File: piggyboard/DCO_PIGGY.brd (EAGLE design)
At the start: 100 x 22 mm, 7 parts, among them P1 100KB, P2 100KB, P3 100KB

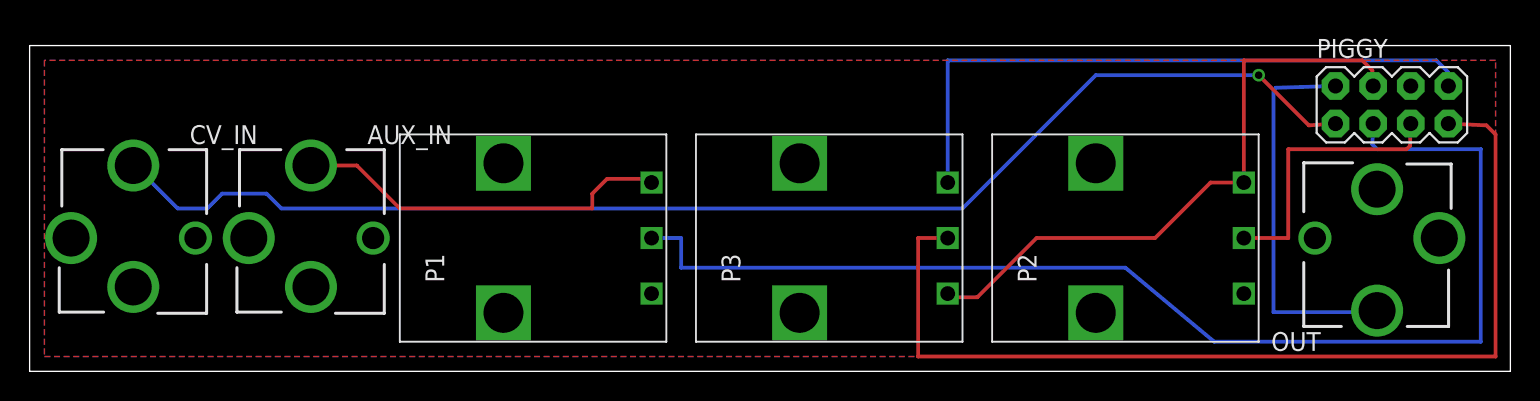
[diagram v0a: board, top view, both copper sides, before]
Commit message: Changed isolation settings on ground planes for piggy back board
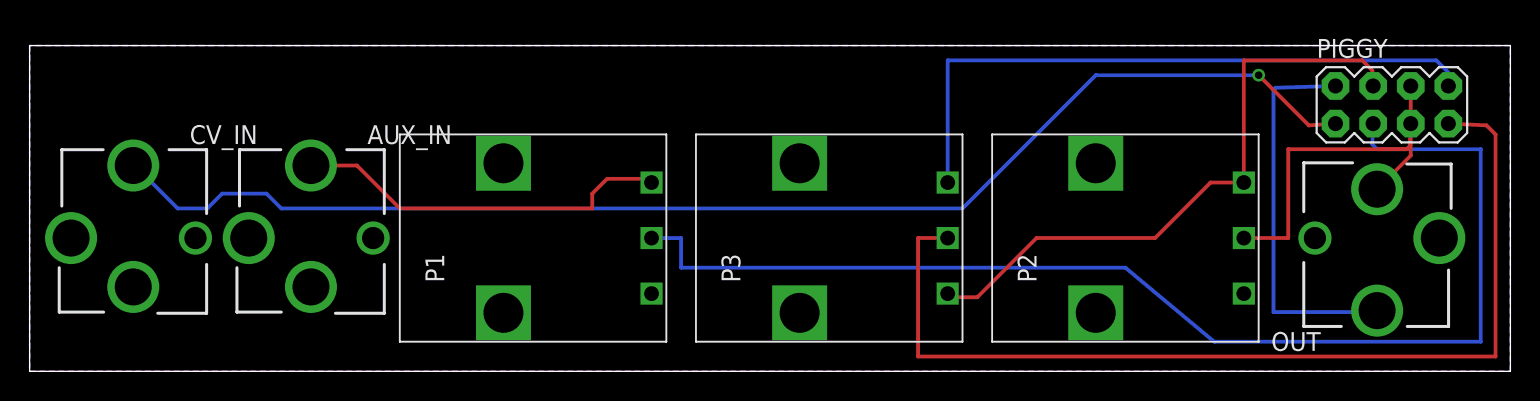
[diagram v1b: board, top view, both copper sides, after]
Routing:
- net GND: track 0.00 -> 7.91 mm
- added copper zone on layer 1, net GND
- added copper zone on layer 16, net N$1
- removed copper zone on layer 1, net N$1
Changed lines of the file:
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@@
 <setting verticaltext="up"/>
 </settings>
-<grid distance="1" unitdist="mm" unit="mm" style="lines" multiple="1" display="yes" altdistance="0.1" altunitdist="mm" altunit="mm"/>
+<grid distance="0.05" unitdist="inch" unit="inch" style="lines" multiple="1" display="yes" altdistance="0.005" altunitdist="inch" altunit="inch"/>
 <layers>
 <layer number="1" name="Top" color="4" fill="1" visible="yes" active="yes"/>
@@
 <contactref element="P1" pad="1"/>
 <contactref element="P2" pad="1"/>
-<polygon width="0.254" layer="16">
-<vertex x="1" y="21"/>
-<vertex x="1" y="1"/>
-<vertex x="99" y="1"/>
-<vertex x="99" y="21"/>
+<polygon width="0.254" layer="16" isolate="0.254">
+<vertex x="0" y="22"/>
+<vertex x="0" y="0"/>
+<vertex x="100" y="0"/>
+<vertex x="100" y="22"/>
 </polygon>
+<polygon width="0.254" layer="1" isolate="0.254">
+<vertex x="0" y="22"/>
+<vertex x="0" y="0"/>
+<vertex x="100" y="0"/>
+<vertex x="100" y="22"/>
+</polygon>
+<wire x1="93.27" y1="19.27" x2="93.27" y2="14.57" width="0.254" layer="1"/>
+<wire x1="93.27" y1="14.57" x2="91" y2="12.3" width="0.254" layer="1"/>
 </signal>
 <signal name="OUT">
@@
 </signal>
 <signal name="N$1">
-<polygon width="0.254" layer="1">
-<vertex x="1" y="21"/>
-<vertex x="1" y="1"/>
-<vertex x="99" y="1"/>
-<vertex x="99" y="21"/>
+<polygon width="0.254" layer="16" isolate="0.254">
+<vertex x="0" y="22"/>
+<vertex x="0" y="0"/>
+<vertex x="100" y="0"/>
+<vertex x="100" y="22"/>
 </polygon>
 </signal>

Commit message: fix for a messed up output jack on the piggy board
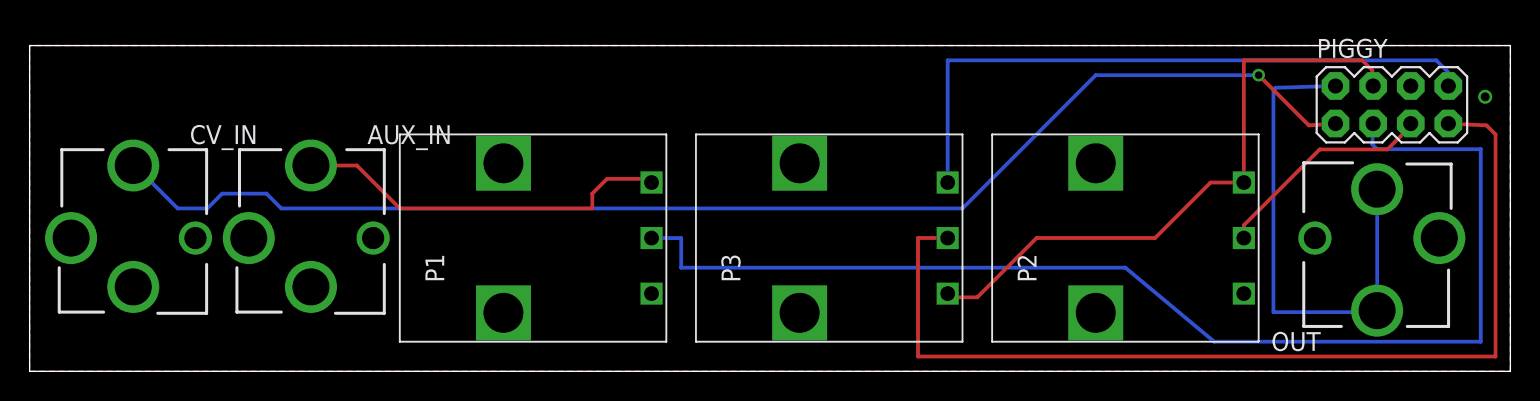
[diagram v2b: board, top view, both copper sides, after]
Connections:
- net GND: no longer OUT.2
- net OUT: now also OUT.2
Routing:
- net OUT: track 26.4 -> 34.6 mm
- net GND: track 7.91 -> 0.00 mm, vias 0 -> 1
- net COARSE: track 18.8 -> 15.1 mm
- removed copper zone on layer 16, net N$1
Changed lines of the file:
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@@
 <?xml version="1.0" encoding="utf-8"?>
 <!DOCTYPE eagle SYSTEM "eagle.dtd">
-<eagle version="6.1">
+<eagle version="6.4">
 <drawing>
 <settings>
@@
 <setting verticaltext="up"/>
 </settings>
-<grid distance="0.05" unitdist="inch" unit="inch" style="lines" multiple="1" display="yes" altdistance="0.005" altunitdist="inch" altunit="inch"/>
+<grid distance="1" unitdist="mm" unit="mm" style="lines" multiple="1" display="yes" altdistance="0.1" altunitdist="mm" altunit="mm"/>
 <layers>
 <layer number="1" name="Top" color="4" fill="1" visible="yes" active="yes"/>
@@
 </class>
 </classes>
-<designrules>
+<designrules name="default">
 <description language="de">&lt;b&gt;EAGLE Design Rules&lt;/b&gt;
 &lt;p&gt;
@@
 <contactref element="OUT" pad="1@1"/>
 <contactref element="OUT" pad="1@2"/>
-<contactref element="OUT" pad="2"/>
 <contactref element="P1" pad="1"/>
 <contactref element="P2" pad="1"/>
-<polygon width="0.254" layer="16" isolate="0.254">
-<vertex x="0" y="22"/>
-<vertex x="0" y="0"/>
-<vertex x="100" y="0"/>
-<vertex x="100" y="22"/>
-</polygon>
 <polygon width="0.254" layer="1" isolate="0.254">
 <vertex x="0" y="22"/>
@@
 <vertex x="100" y="22"/>
 </polygon>
-<wire x1="93.27" y1="19.27" x2="93.27" y2="14.57" width="0.254" layer="1"/>
-<wire x1="93.27" y1="14.57" x2="91" y2="12.3" width="0.254" layer="1"/>
+<via x="98.298" y="18.542" extent="1-16" drill="0.6" shape="square"/>
+<polygon width="0.254" layer="16">
+<vertex x="0" y="22"/>
+<vertex x="0" y="0"/>
+<vertex x="100" y="0"/>
+<vertex x="100" y="22"/>
+</polygon>
 </signal>
 <signal name="OUT">
@@
 <wire x1="84" y1="4" x2="91" y2="4" width="0.254" layer="16"/>
 <wire x1="91" y1="4.1" x2="91" y2="4" width="0.254" layer="16"/>
+<contactref element="OUT" pad="2"/>
+<wire x1="91" y1="12.3" x2="91" y2="4.1" width="0.254" layer="16"/>
 </signal>
 <signal name="CV_IN">
@@
 <contactref element="PIGGY" pad="5"/>
 <contactref element="P2" pad="2"/>
-<wire x1="93.27" y1="16.73" x2="93.22" y2="15.22" width="0.254" layer="1"/>
-<wire x1="93.22" y1="15.22" x2="93" y2="15" width="0.254" layer="1"/>
-<wire x1="93" y1="15" x2="85" y2="15" width="0.254" layer="1"/>
-<wire x1="85" y1="15" x2="85" y2="9" width="0.254" layer="1"/>
-<wire x1="85" y1="9" x2="82" y2="9" width="0.254" layer="1"/>
+<wire x1="82" y1="9" x2="82" y2="9.864" width="0.254" layer="1"/>
+<wire x1="82" y1="9.864" x2="87.122" y2="14.986" width="0.254" layer="1"/>
+<wire x1="87.122" y1="14.986" x2="91.694" y2="14.986" width="0.254" layer="1"/>
+<wire x1="91.694" y1="14.986" x2="92.964" y2="16.256" width="0.254" layer="1"/>
+<wire x1="92.964" y1="16.256" x2="92.964" y2="16.424" width="0.254" layer="1"/>
+<wire x1="92.964" y1="16.424" x2="93.27" y2="16.73" width="0.254" layer="1"/>
 </signal>
 <signal name="FINE">
@@
 <wire x1="42" y1="13" x2="42" y2="12.75" width="0.254" layer="1"/>
 </signal>
-<signal name="N$1">
-<polygon width="0.254" layer="16" isolate="0.254">
-<vertex x="0" y="22"/>
-<vertex x="0" y="0"/>
-<vertex x="100" y="0"/>
-<vertex x="100" y="22"/>
-</polygon>
-</signal>
 </signals>

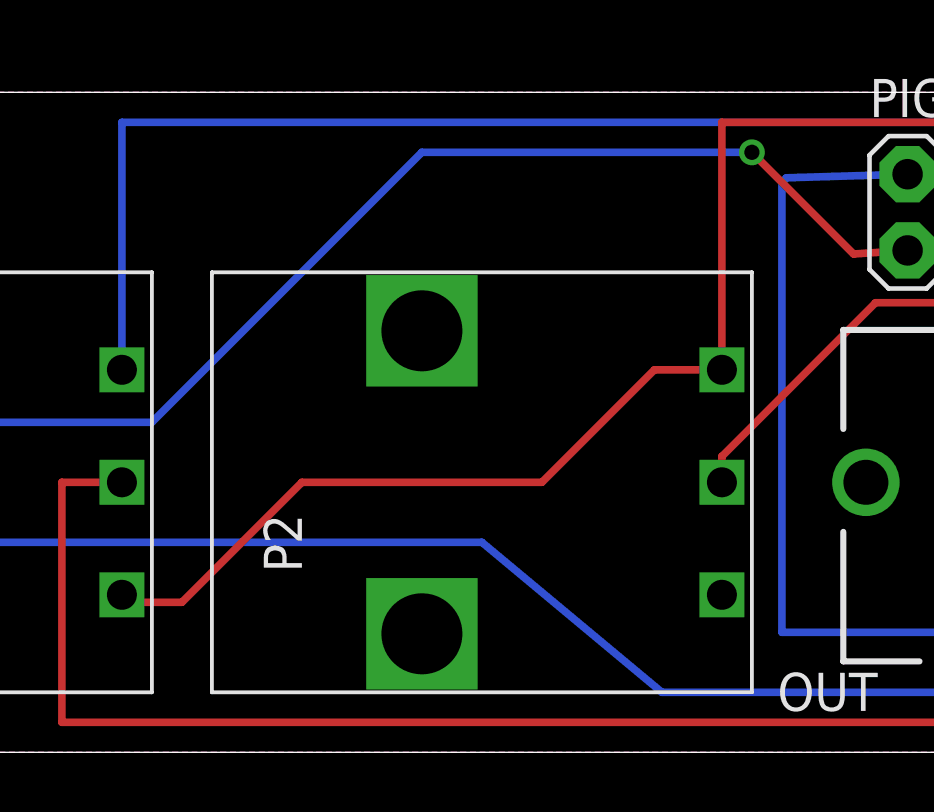
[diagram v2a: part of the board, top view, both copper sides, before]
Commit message: fixed footprint
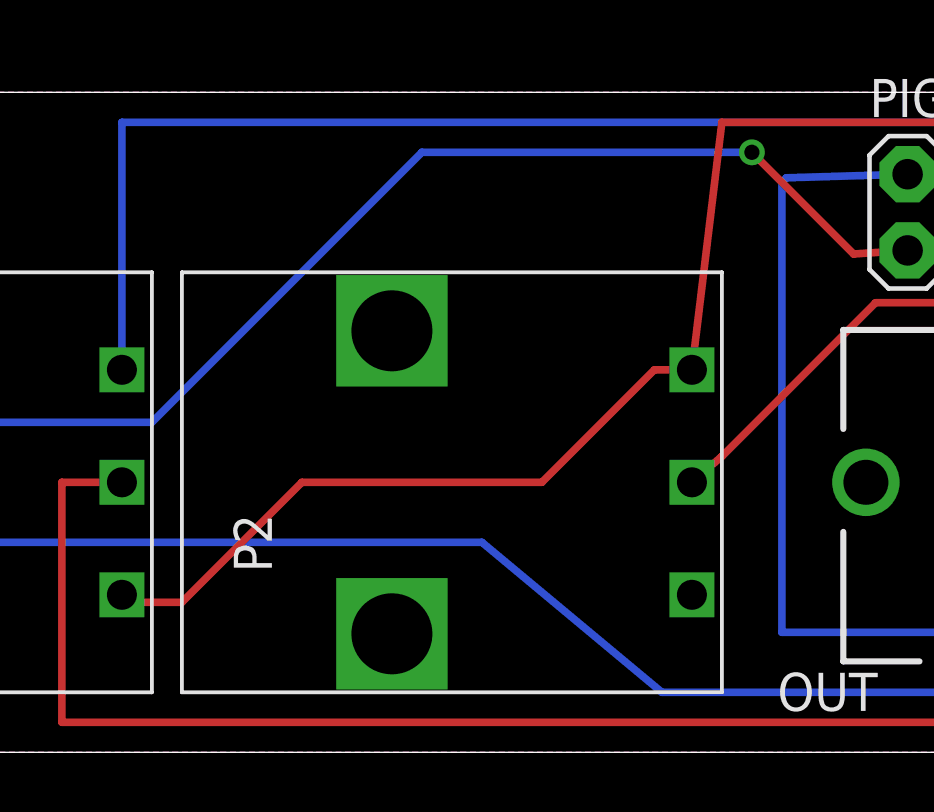
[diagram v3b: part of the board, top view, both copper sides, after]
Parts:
- moved P2 6.00 mm to (71.0, 9.00)
- moved P1 5.00 mm to (32.0, 9.00)
- moved P3 5.00 mm to (52.0, 9.00)
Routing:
- net +5V: track 41.7 -> 40.8 mm
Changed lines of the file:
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@@
 <element name="AUX_IN" library="erthenvar" package="ERTHENVAR-JACK" value="AUDIO-JACKERTHENVAR" x="19" y="9"/>
 <element name="OUT" library="erthenvar" package="ERTHENVAR-JACK" value="AUDIO-JACKERTHENVAR" x="91" y="9" rot="R180"/>
-<element name="P1" library="SparkFun" package="PDB12" value="100KB" x="37" y="9" rot="R90"/>
-<element name="P2" library="SparkFun" package="PDB12" value="100KB" x="77" y="9" rot="R90"/>
-<element name="P3" library="SparkFun" package="PDB12" value="100KB" x="57" y="9" rot="R90"/>
+<element name="P1" library="SparkFun" package="PDB12" value="100KB" x="32" y="9" rot="R90"/>
+<element name="P2" library="SparkFun" package="PDB12" value="100KB" x="71" y="9" rot="R90"/>
+<element name="P3" library="SparkFun" package="PDB12" value="100KB" x="52" y="9" rot="R90"/>
 </elements>
 <signals>
@@
 <wire x1="90.68" y1="20.32" x2="90" y2="21" width="0.254" layer="1"/>
 <wire x1="90" y1="21" x2="82" y2="21" width="0.254" layer="1"/>
-<wire x1="82" y1="21" x2="82" y2="12.75" width="0.254" layer="1"/>
-<wire x1="82" y1="12.75" x2="79.75" y2="12.75" width="0.254" layer="1"/>
+<wire x1="82" y1="21" x2="81" y2="12.75" width="0.254" layer="1"/>
+<wire x1="81" y1="12.75" x2="79.75" y2="12.75" width="0.254" layer="1"/>
 <wire x1="79.75" y1="12.75" x2="76" y2="9" width="0.254" layer="1"/>
 <wire x1="76" y1="9" x2="68" y2="9" width="0.254" layer="1"/>
@@
 <contactref element="PIGGY" pad="5"/>
 <contactref element="P2" pad="2"/>
-<wire x1="82" y1="9" x2="82" y2="9.864" width="0.254" layer="1"/>
+<wire x1="81" y1="9" x2="82" y2="9.864" width="0.254" layer="1"/>
 <wire x1="82" y1="9.864" x2="87.122" y2="14.986" width="0.254" layer="1"/>
 <wire x1="87.122" y1="14.986" x2="91.694" y2="14.986" width="0.254" layer="1"/>

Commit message: Fix for design flaw - fine pitch control was attached backwards.
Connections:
- net +5V: now also P3.3; no longer P3.1
- net -5V: now also P3.1; no longer P3.3
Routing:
- net -5V: track 43.3 -> 53.8 mm, vias 0 -> 1
- net FINE: track 67.4 -> 61.7 mm
- net +5V: track 40.8 -> 39.5 mm
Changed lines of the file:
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@@
 <setting verticaltext="up"/>
 </settings>
-<grid distance="1" unitdist="mm" unit="mm" style="lines" multiple="1" display="yes" altdistance="0.1" altunitdist="mm" altunit="mm"/>
+<grid distance="0.01" unitdist="inch" unit="inch" style="lines" multiple="1" display="yes" altdistance="0.005" altunitdist="inch" altunit="inch"/>
 <layers>
 <layer number="1" name="Top" color="4" fill="1" visible="yes" active="yes"/>
@@
 <contactref element="PIGGY" pad="4"/>
 <contactref element="P2" pad="3"/>
-<contactref element="P3" pad="1"/>
 <wire x1="90.73" y1="19.27" x2="90.68" y2="20.32" width="0.254" layer="1"/>
 <wire x1="90.68" y1="20.32" x2="90" y2="21" width="0.254" layer="1"/>
 <wire x1="90" y1="21" x2="82" y2="21" width="0.254" layer="1"/>
 <wire x1="82" y1="21" x2="81" y2="12.75" width="0.254" layer="1"/>
-<wire x1="81" y1="12.75" x2="79.75" y2="12.75" width="0.254" layer="1"/>
-<wire x1="79.75" y1="12.75" x2="76" y2="9" width="0.254" layer="1"/>
-<wire x1="76" y1="9" x2="68" y2="9" width="0.254" layer="1"/>
-<wire x1="68" y1="9" x2="64" y2="5" width="0.254" layer="1"/>
-<wire x1="64" y1="5" x2="62" y2="5" width="0.254" layer="1"/>
-<wire x1="62" y1="5.25" x2="62" y2="5" width="0.254" layer="1"/>
+<contactref element="P3" pad="3"/>
+<wire x1="62" y1="12.75" x2="63.45" y2="12.75" width="0.254" layer="1"/>
+<wire x1="63.45" y1="12.75" x2="66.04" y2="10.16" width="0.254" layer="1"/>
+<wire x1="66.04" y1="10.16" x2="76.2" y2="10.16" width="0.254" layer="1"/>
+<wire x1="76.2" y1="10.16" x2="78.74" y2="12.7" width="0.254" layer="1"/>
+<wire x1="78.74" y1="12.7" x2="80.95" y2="12.7" width="0.254" layer="1"/>
+<wire x1="80.95" y1="12.7" x2="81" y2="12.75" width="0.254" layer="1"/>
 </signal>
 <signal name="-5V">
 <contactref element="PIGGY" pad="8"/>
-<contactref element="P3" pad="3"/>
 <wire x1="95.81" y1="19.27" x2="95.76" y2="20.24" width="0.254" layer="16"/>
 <wire x1="95.76" y1="20.24" x2="95" y2="21" width="0.254" layer="16"/>
 <wire x1="95" y1="21" x2="62" y2="21" width="0.254" layer="16"/>
-<wire x1="62" y1="21" x2="62" y2="12.75" width="0.254" layer="16"/>
+<contactref element="P3" pad="1"/>
+<wire x1="62" y1="5.25" x2="61.044" y2="5.25" width="0.254" layer="1"/>
+<wire x1="61.044" y1="5.25" x2="59.182" y2="7.112" width="0.254" layer="1"/>
+<wire x1="59.182" y1="7.112" x2="59.182" y2="18.034" width="0.254" layer="1"/>
+<wire x1="59.182" y1="18.182" x2="59.182" y2="18.034" width="0.254" layer="1"/>
+<via x="59.182" y="18.034" extent="1-16" drill="0.508"/>
+<wire x1="59.182" y1="18.034" x2="59.182" y2="18.182" width="0.254" layer="16"/>
+<wire x1="59.182" y1="18.182" x2="62" y2="21" width="0.254" layer="16"/>
 </signal>
 <signal name="COARSE">
@@
 <wire x1="98.39" y1="16.61" x2="99" y2="16" width="0.254" layer="1"/>
 <wire x1="99" y1="16" x2="99" y2="1" width="0.254" layer="1"/>
-<wire x1="99" y1="1" x2="60" y2="1" width="0.254" layer="1"/>
-<wire x1="60" y1="1" x2="60" y2="9" width="0.254" layer="1"/>
-<wire x1="60" y1="9" x2="62" y2="9" width="0.254" layer="1"/>
+<wire x1="99" y1="1" x2="65.786" y2="1" width="0.254" layer="1"/>
+<wire x1="62" y1="9" x2="62.882" y2="9" width="0.254" layer="1"/>
+<wire x1="62.882" y1="9" x2="63.754" y2="8.128" width="0.254" layer="1"/>
+<wire x1="63.754" y1="8.128" x2="63.754" y2="3.032" width="0.254" layer="1"/>
+<wire x1="63.754" y1="3.032" x2="65.786" y2="1" width="0.254" layer="1"/>
 </signal>
 <signal name="N$3">
